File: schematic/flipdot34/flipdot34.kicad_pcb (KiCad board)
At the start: 2 copper layers, 11 parts, among them J1 FlipDot matrix, J2 I2C bus, J3 Config Jumpers, J4 Power 24V, U1 74HC595, U2 74HC595

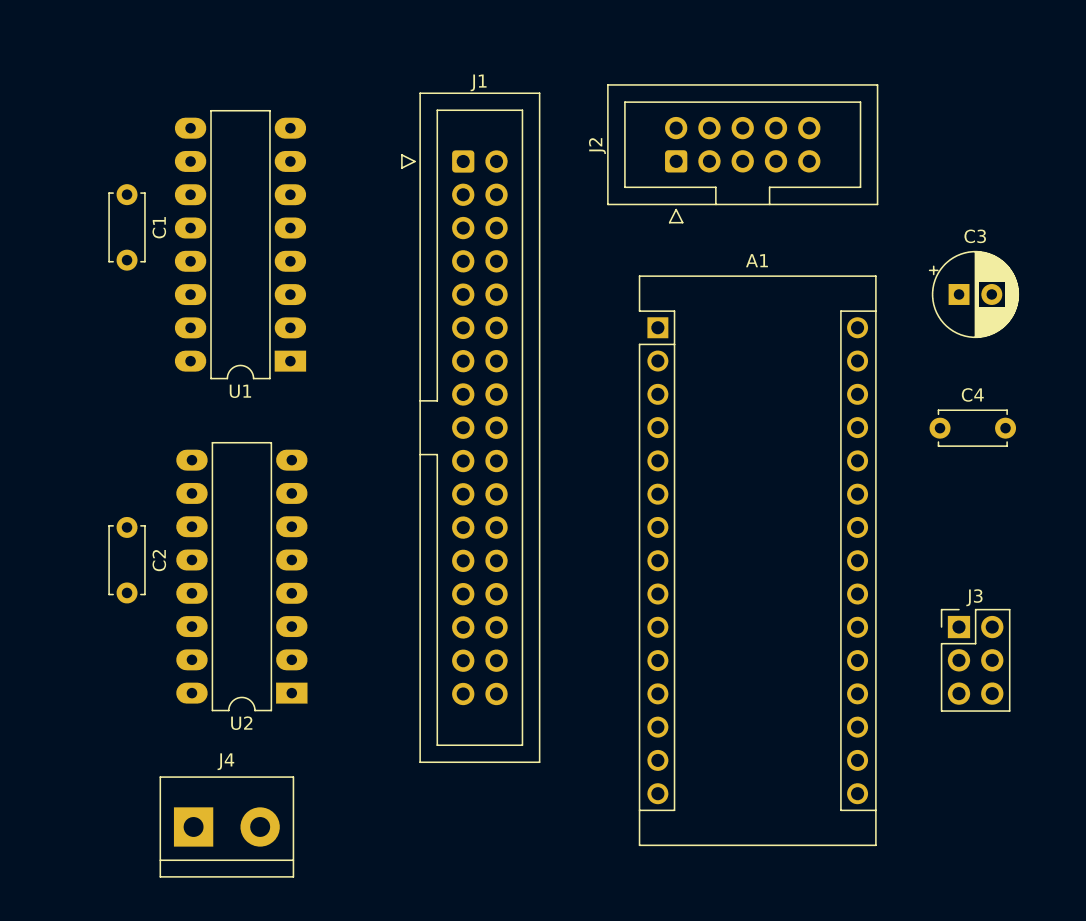
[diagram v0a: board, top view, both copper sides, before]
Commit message: Add mounting holes
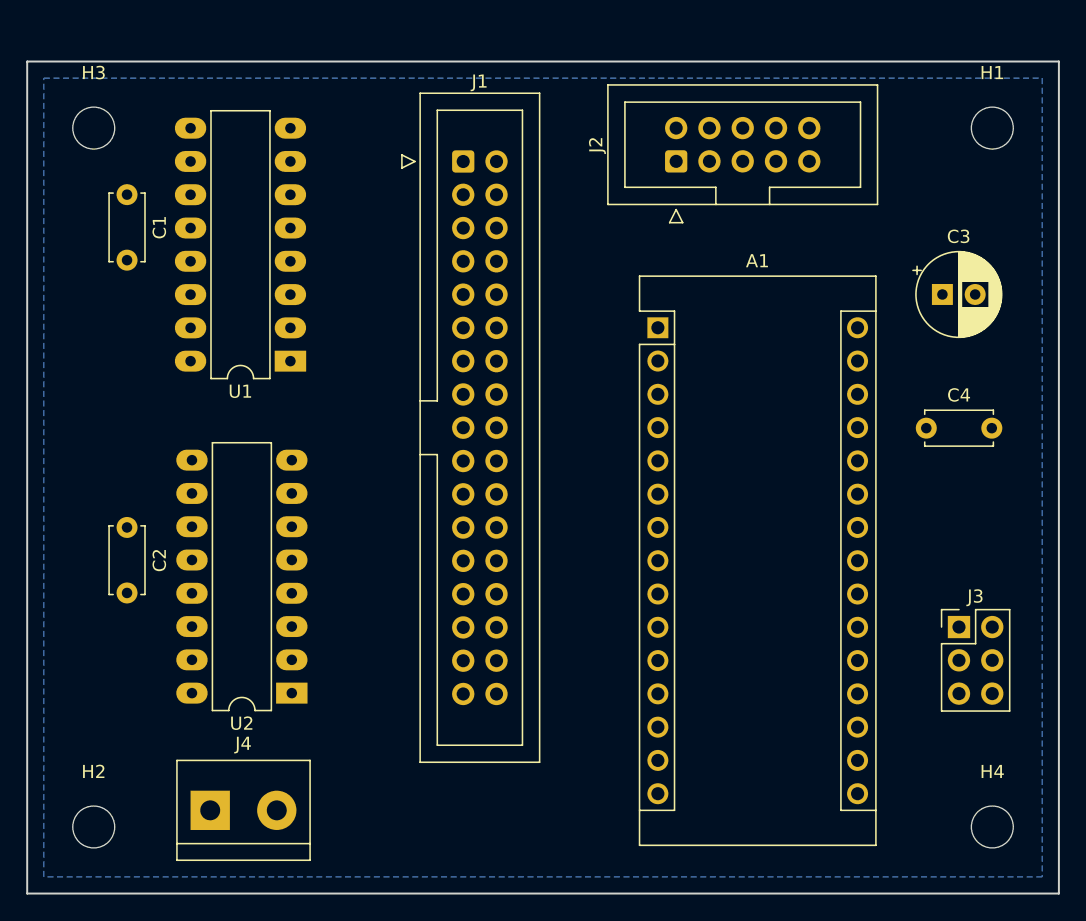
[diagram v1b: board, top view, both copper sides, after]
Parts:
- added H1: MountingHole, MountingHole:MountingHole_3.2mm_M3, F.Cu at (157.5, 76.2)
- added H2: MountingHole, MountingHole:MountingHole_3.2mm_M3, F.Cu at (88.9, 129.5)
- added H3: MountingHole, MountingHole:MountingHole_3.2mm_M3, F.Cu at (88.9, 76.2)
- added H4: MountingHole, MountingHole:MountingHole_3.2mm_M3, F.Cu at (157.5, 129.5)
- moved J4 1.80 mm to (97.8, 128.3)
- moved C3 1.27 mm to (153.7, 88.9)
- moved C4 1.05 mm to (152.4, 99.1)
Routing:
- added copper zone on B.Cu, net GND
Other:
- board outline added: 78.7 x 63.5 mm
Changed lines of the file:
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@@
     )
+  )
+  (footprint "MountingHole:MountingHole_3.2mm_M3" (layer "F.Cu")
+    (at 157.48 76.2)
+    (descr "Mounting Hole 3.2mm, no annular, M3")
+    (tags "mounting hole 3.2mm no annular m3")
+    (property "Sheetfile" "flipdot34.kicad_sch")
+    (property "Sheetname" "")
+    (property "exclude_from_bom" "")
+    (attr exclude_from_pos_files exclude_from_bom)
+    (fp_text reference "H1" (at 0 -4.2) (layer "F.SilkS")
+      (effects (font (size 1 1) (thickness 0.15)))
+    )
+    (fp_text value "MountingHole" (at 0 4.2) (layer "F.Fab")
+      (effects (font (size 1 1) (thickness 0.15)))
+    )
+    (fp_text user "${REFERENCE}" (at 0.3 0) (layer "F.Fab")
+      (effects (font (size 1 1) (thickness 0.15)))
+    )
+    (fp_circle (center 0 0) (end 3.2 0) (layer "Cmts.User") (width 0.15) (fill none))
+    (fp_circle (center 0 0) (end 3.45 0) (layer "F.CrtYd") (width 0.05) (fill none))
+    (pad "" np_thru_hole circle locked (at 0 0) (size 3.2 3.2) (drill 3.2) (layers F&B.Cu *.Mask)
+      (clearance 3))
   )
   (footprint "Connector_IDC:IDC-Header_2x05_P2.54mm_Vertical" (layer "F.Cu")
@@
   )
   (footprint "Capacitor_THT:CP_Radial_D6.3mm_P2.50mm" (layer "F.Cu")
-    (at 154.94 88.9)
+    (at 153.67 88.9)
     (descr "CP, Radial series, Radial, pin pitch=2.50mm, , diameter=6.3mm, Electrolytic Capacitor")
     (tags "CP Radial series Radial pin pitch 2.50mm  diameter 6.3mm Electrolytic Capacitor")
@@
     )
   )
+  (footprint "MountingHole:MountingHole_3.2mm_M3" (layer "F.Cu")
+    (at 157.48 129.54)
+    (descr "Mounting Hole 3.2mm, no annular, M3")
+    (tags "mounting hole 3.2mm no annular m3")
+    (property "Sheetfile" "flipdot34.kicad_sch")
+    (property "Sheetname" "")
+    (property "exclude_from_bom" "")
+    (attr exclude_from_pos_files exclude_from_bom)
+    (fp_text reference "H4" (at 0 -4.2) (layer "F.SilkS")
+      (effects (font (size 1 1) (thickness 0.15)))
+    )
+    (fp_text value "MountingHole" (at 0 4.2) (layer "F.Fab")
+      (effects (font (size 1 1) (thickness 0.15)))
+    )
+    (fp_text user "${REFERENCE}" (at 0.3 0) (layer "F.Fab")
+      (effects (font (size 1 1) (thickness 0.15)))
+    )
+    (fp_circle (center 0 0) (end 3.2 0) (layer "Cmts.User") (width 0.15) (fill none))
+    (fp_circle (center 0 0) (end 3.45 0) (layer "F.CrtYd") (width 0.05) (fill none))
+    (pad "" np_thru_hole circle locked (at 0 0) (size 3.2 3.2) (drill 3.2) (layers F&B.Cu *.Mask)
+      (clearance 3))
+  )
   (footprint "Capacitor_THT:C_Disc_D5.0mm_W2.5mm_P5.00mm" (layer "F.Cu")
-    (at 153.487581 99.102894)
+    (at 152.44 99.102894)
     (descr "C, Disc series, Radial, pin pitch=5.00mm, , diameter*width=5*2.5mm^2, Capacitor, http://cdn-reichelt.de/documents/datenblatt/B300/DS_KERKO_TC.pdf")
     (tags "C Disc series Radial pin pitch 5.00mm  diameter 5mm width 2.5mm Capacitor")
@@
   )
   (footprint "TerminalBlock:TerminalBlock_bornier-2_P5.08mm" (layer "F.Cu")
-    (at 96.52 129.54)
+    (at 97.79 128.27)
     (descr "simple 2-pin terminal block, pitch 5.08mm, revamped version of bornier2")
     (tags "terminal block bornier2")
@@
       (rotate (xyz 0 0 0))
     )
+  )
+  (footprint "MountingHole:MountingHole_3.2mm_M3" (layer "F.Cu")
+    (at 88.9 76.2)
+    (descr "Mounting Hole 3.2mm, no annular, M3")
+    (tags "mounting hole 3.2mm no annular m3")
+    (property "Sheetfile" "flipdot34.kicad_sch")
+    (property "Sheetname" "")
+    (property "exclude_from_bom" "")
+    (attr exclude_from_pos_files exclude_from_bom)
+    (fp_text reference "H3" (at 0 -4.2) (layer "F.SilkS")
+      (effects (font (size 1 1) (thickness 0.15)))
+    )
+    (fp_text value "MountingHole" (at 0 4.2) (layer "F.Fab")
+      (effects (font (size 1 1) (thickness 0.15)))
+    )
+    (fp_text user "${REFERENCE}" (at 0.3 0) (layer "F.Fab")
+      (effects (font (size 1 1) (thickness 0.15)))
+    )
+    (fp_circle (center 0 0) (end 3.2 0) (layer "Cmts.User") (width 0.15) (fill none))
+    (fp_circle (center 0 0) (end 3.45 0) (layer "F.CrtYd") (width 0.05) (fill none))
+    (pad "" np_thru_hole circle locked (at 0 0) (size 3.2 3.2) (drill 3.2) (layers F&B.Cu *.Mask)
+      (clearance 3))
   )
   (footprint "Capacitor_THT:C_Disc_D5.0mm_W2.5mm_P5.00mm" (layer "F.Cu")
@@
       (rotate (xyz 0 0 0))
     )
+  )
+  (footprint "MountingHole:MountingHole_3.2mm_M3" (layer "F.Cu")
+    (at 88.9 129.54)
+    (descr "Mounting Hole 3.2mm, no annular, M3")
+    (tags "mounting hole 3.2mm no annular m3")
+    (property "Sheetfile" "flipdot34.kicad_sch")
+    (property "Sheetname" "")
+    (property "exclude_from_bom" "")
+    (attr exclude_from_pos_files exclude_from_bom)
+    (fp_text reference "H2" (at 0 -4.2) (layer "F.SilkS")
+      (effects (font (size 1 1) (thickness 0.15)))
+    )
+    (fp_text value "MountingHole" (at 0 4.2) (layer "F.Fab")
+      (effects (font (size 1 1) (thickness 0.15)))
+    )
+    (fp_text user "${REFERENCE}" (at 0.3 0) (layer "F.Fab")
+      (effects (font (size 1 1) (thickness 0.15)))
+    )
+    (fp_circle (center 0 0) (end 3.2 0) (layer "Cmts.User") (width 0.15) (fill none))
+    (fp_circle (center 0 0) (end 3.45 0) (layer "F.CrtYd") (width 0.05) (fill none))
+    (pad "" np_thru_hole circle locked (at 0 0) (size 3.2 3.2) (drill 3.2) (layers F&B.Cu *.Mask)
+      (clearance 3))
   )
   (footprint "Package_DIP:DIP-16_W7.62mm_LongPads" (layer "F.Cu")
@@
     )
   )
-  (gr_rect (start 83.82 71.12) (end 162.56 134.62) (layer "Dwgs.User") (width 0.15) (fill none))
+  (gr_rect (start 83.82 71.12) (end 162.56 134.62) (layer "Edge.Cuts") (width 0.15) (fill none))
   (dimension (type aligned) (layer "Dwgs.User")
     (pts (xy 83.82 134.62) (xy 162.56 134.62))
@@
     (style (thickness 0.15) (arrow_length 1.27) (text_position_mode 0) (extension_height 0.58642) (extension_offset 0.5) keep_text_aligned)
   )
+  (zone (net 7) (net_name "GND") (layer "B.Cu") (hatch edge 0.508)
+    (connect_pads yes (clearance 0.508))
+    (min_thickness 0.254) (filled_areas_thickness no)
+    (fill yes (thermal_gap 0.508) (thermal_bridge_width 0.508))
+    (polygon
+      (pts
+        (xy 161.29 133.35)
+        (xy 85.09 133.35)
+        (xy 85.09 72.39)
+        (xy 161.29 72.39)
+      )
+    )
+  )
 )

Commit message: DRC tests pass
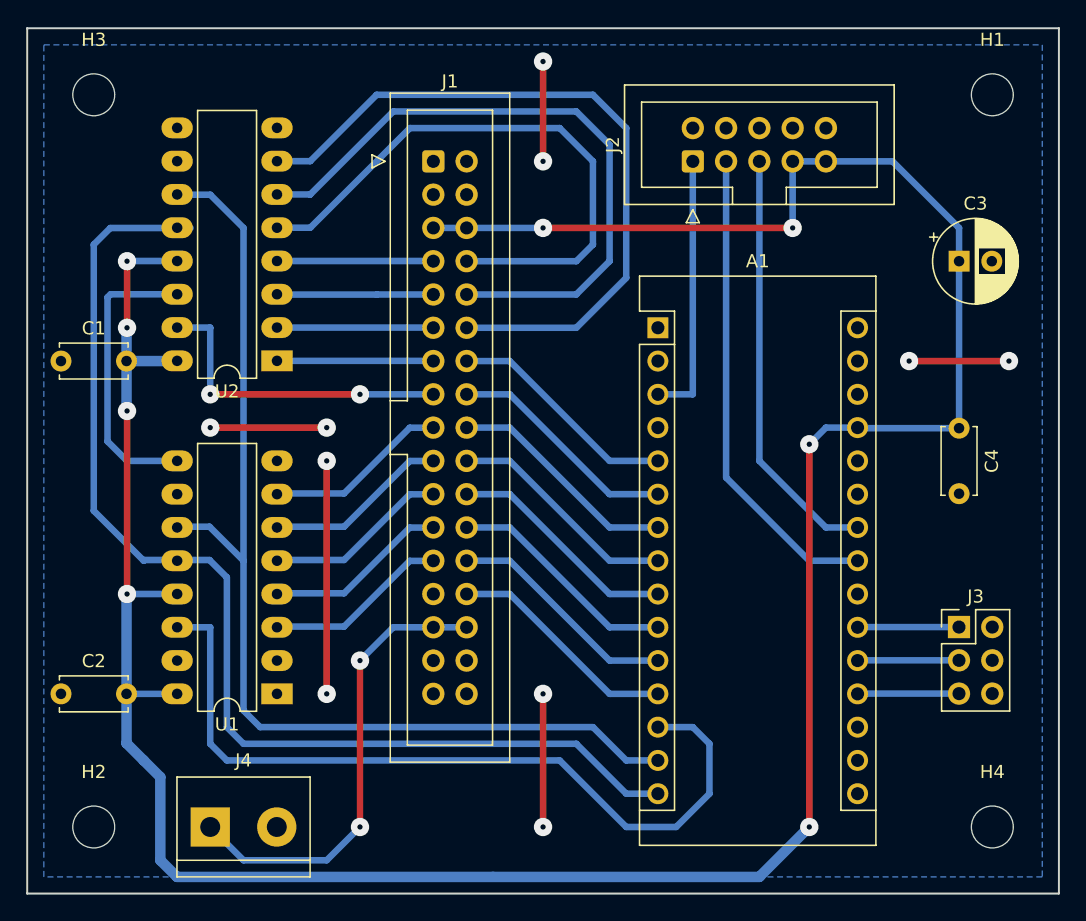
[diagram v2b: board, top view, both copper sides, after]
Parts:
- moved U1 25.4 mm to (102.9, 119.4)
- moved U2 25.4 mm to (102.9, 94.0)
- moved C1 13.7 mm to (86.4, 94.0), turned to 0 degrees
- moved C2 13.7 mm to (86.4, 119.4), turned to 0 degrees
- moved C3 2.84 mm to (154.9, 86.4)
- moved H1 2.54 mm to (157.5, 73.7)
- moved H3 2.54 mm to (88.9, 73.7)
- moved C4 2.50 mm to (154.9, 99.1), turned to -90 degrees
- moved J1 2.28 mm to (114.8, 78.7)
- moved J2 1.27 mm to (134.6, 78.7)
- moved J4 1.27 mm to (97.8, 129.5)
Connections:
- U1 pad 1: B0-X -> unconnected-(U1-Pad1)
- U1 pad 15: B1-X -> unconnected-(U1-Pad15)
- U1 pad 2: A2-X -> unconnected-(U1-Pad2)
- U1 pad 3: A1-X -> B1-Y
- U1 pad 4: A0-X -> B0-Y
- U1 pad 5: DATA-X -> A2-Y
- U1 pad 6: ENABLE-Y-SET -> A1-Y
- U1 pad 7: ENABLE-Y-RESET -> A0-Y
- U2 pad 1: unconnected-(U2-Pad1) -> B0-X
- U2 pad 15: unconnected-(U2-Pad15) -> B1-X
- U2 pad 2: unconnected-(U2-Pad2) -> A2-X
- U2 pad 3: B1-Y -> A1-X
- U2 pad 4: B0-Y -> A0-X
- U2 pad 5: A2-Y -> DATA-X
- U2 pad 6: A1-Y -> ENABLE-Y-SET
- U2 pad 7: A0-Y -> ENABLE-Y-RESET
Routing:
- net Vin: track 0.00 -> 217.6 mm, vias 0 -> 8
- net Net-(A1-Pad15): track 0.00 -> 87.0 mm
- net Net-(A1-Pad14): track 0.00 -> 80.1 mm
- net Net-(A1-Pad13): track 0.00 -> 61.5 mm
- net ENABLE-Y-RESET: track 0.00 -> 55.0 mm
- net GND: track 0.00 -> 52.1 mm, vias 0 -> 10
- net ENABLE-Y-SET: track 0.00 -> 49.9 mm
- net DATA-X: track 0.00 -> 44.8 mm
- net SDA: track 0.00 -> 36.8 mm
- net Net-(J1-Pad29): track 0.00 -> 35.4 mm, vias 0 -> 2
- net SCL: track 0.00 -> 32.5 mm
- net B1-X: track 0.00 -> 24.6 mm, vias 0 -> 2
- net Net-(U1-Pad9): track 0.00 -> 22.3 mm
- net RESET: track 0.00 -> 20.4 mm
- net ENABLE-X-7: track 0.00 -> 17.8 mm
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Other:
- board size 78.7 x 63.5 mm -> 78.7 x 66 mm
